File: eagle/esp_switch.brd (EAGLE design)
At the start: 100 x 80 mm, 20 parts, among them IC1 LT1117-3.3V

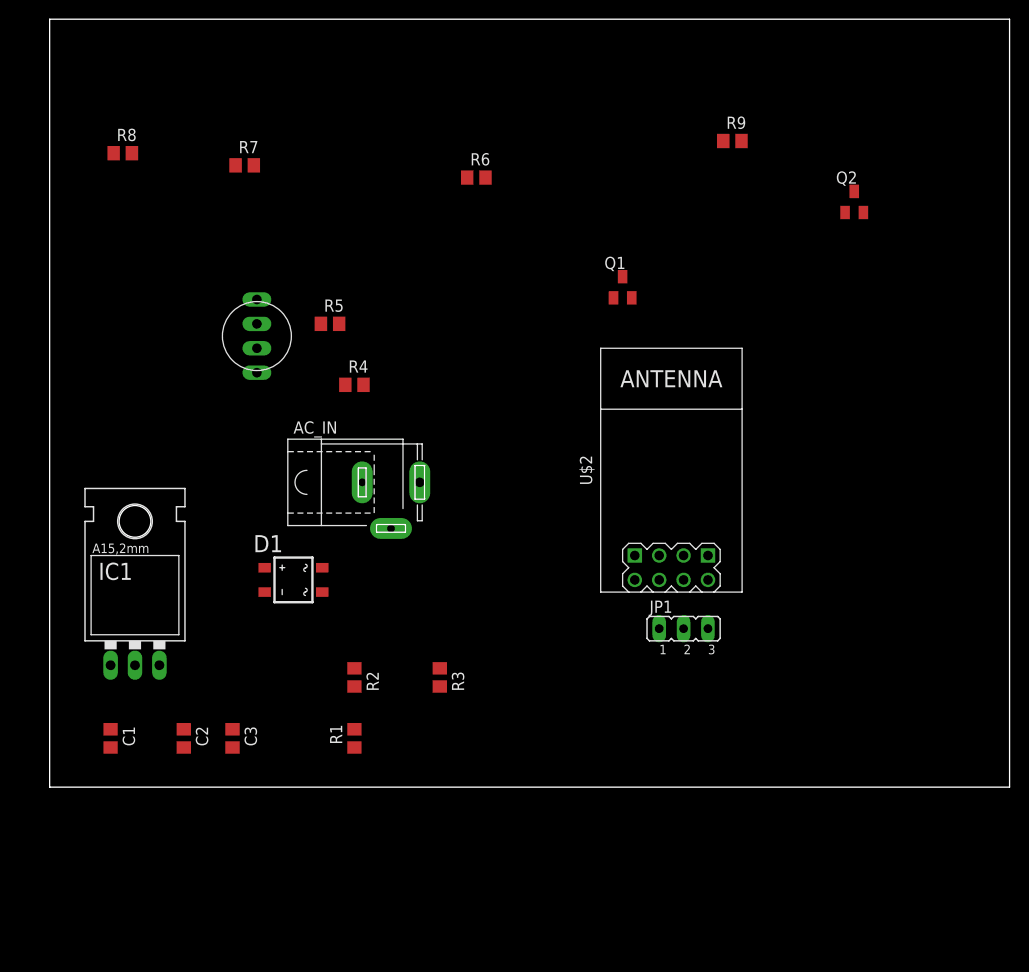
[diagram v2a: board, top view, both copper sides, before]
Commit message: modified brd size for case and add out port,SSR to sch, brd
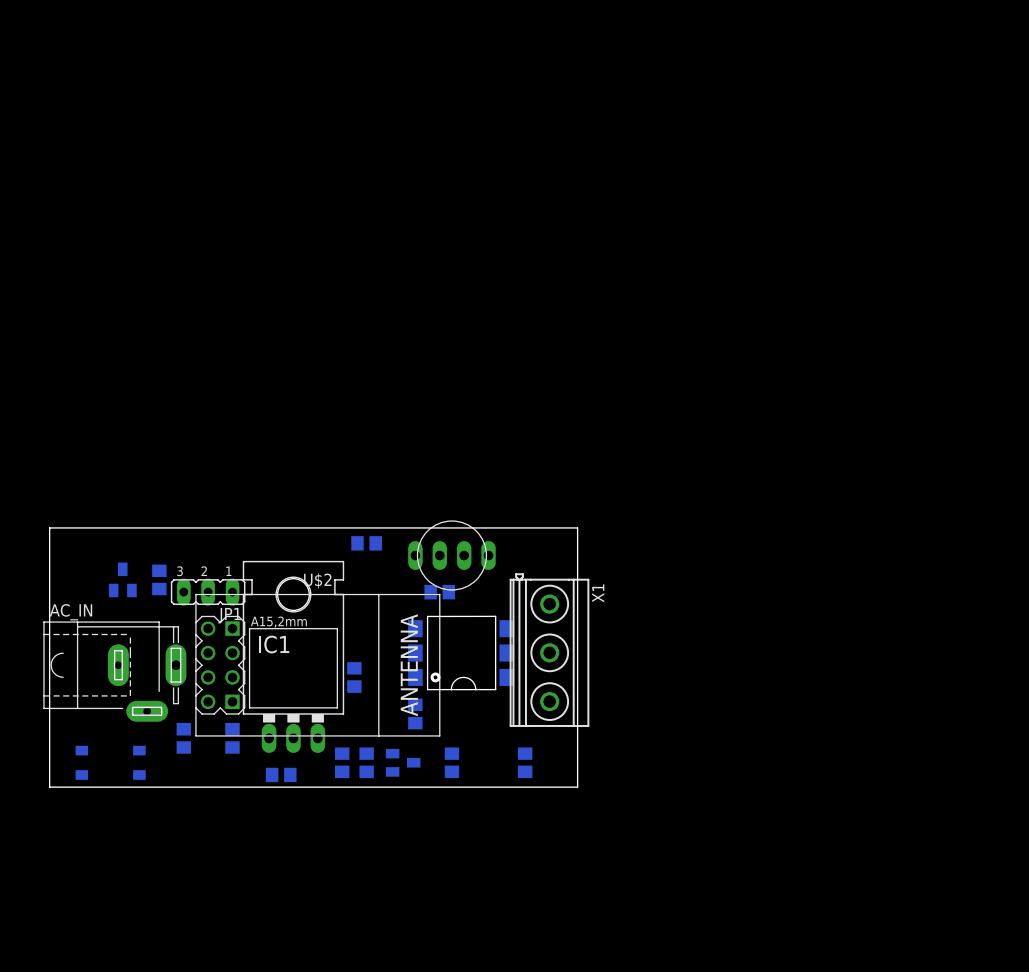
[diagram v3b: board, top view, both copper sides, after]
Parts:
- removed U$1: RGB_LEDA, covek:RGB_LED
- added LH1500: (no value), LH1500:LH1500
- added RGBLED5MM: RGB_LEDA, covek:RGB_LED
- added X1: MKDSN1,5/3-5,08, con-phoenix-508:MKDSN1,5/3-5,08
- AC_IN: value 6V AC -> 5V AC
- moved Q2 75.0 mm to (36.8, 2.54), flipped to the bottom, turned to 90 degrees
- moved R8 68.4 mm to (33.0, 2.54), flipped to the bottom, turned to 90 degrees
- moved R9 68.2 mm to (38.1, 7.62), flipped to the bottom, turned to 270 degrees
- moved R7 63.1 mm to (30.5, 2.54), flipped to the bottom, turned to 270 degrees
- moved Q1 60.3 mm to (7.62, 21.6), flipped to the bottom
- moved R6 53.4 mm to (11.4, 21.6), flipped to the bottom, turned to 90 degrees
- moved JP1 49.7 mm to (16.5, 20.3), turned to 180 degrees
- moved C1 43.3 mm to (49.5, 2.54), flipped to the bottom
- moved U$2 42.1 mm to (27.9, 12.7), turned to 0 degrees
- moved AC_IN 31.8 mm to (10.2, 12.7)
- moved D1 26.9 mm to (6.35, 2.54), flipped to the bottom
- moved R4 23.3 mm to (40.6, 20.3), flipped to the bottom
- moved R5 23.2 mm to (33.0, 25.4), flipped to the bottom
- moved IC1 18.2 mm to (25.4, 8.89)
- moved R3 8.98 mm to (41.9, 2.54), flipped to the bottom
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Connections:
- net N$7 renamed 3.3V
- new net 5V: AC_IN.3, D1.AC2
- new net N$18: LH1500.A, R9.1
- new net N$7: LH1500.DC, X1.2
- net N$1: now also D1.AC1; no longer D1.AC2
- net N$11: now also RGBLED5MM.P$2; no longer U$1.P$2
- net N$12: now also RGBLED5MM.P$4; no longer U$1.P$4
- net N$14: now also LH1500.S', X1.1; no longer Q2.2, R8.1
- net N$2: now also LH1500.S, X1.3; no longer AC_IN.3, D1.AC1
- net N$3: now also LH1500.C, RGBLED5MM.P$3
- net N$6: now also Q2.2, R8.1; no longer U$1.P$3
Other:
- board size 100 x 80 mm -> 55 x 27 mm

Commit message: brd modified2
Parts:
- moved X1 49.1 mm to (3.17, 15.9), turned to 90 degrees
- moved D1 38.9 mm to (45.1, 6.35), turned to 0 degrees
- moved AC_IN 34.9 mm to (45.1, 13.3), turned to 180 degrees
- moved R3 24.8 mm to (32.4, 25.4), turned to 180 degrees
- moved R7 24.3 mm to (22.2, 25.4), turned to 0 degrees
- moved JP1 24.1 mm to (36.2, 6.35), turned to 0 degrees
- moved LH1500 23.9 mm to (14.6, 15.9), turned to 0 degrees
- moved R8 23.6 mm to (27.3, 25.4), turned to 0 degrees
- moved C1 22.5 mm to (27.9, 8.89), turned to 90 degrees
- moved R9 21.3 mm to (18.4, 15.9), turned to 180 degrees
- moved Q2 18.9 mm to (23.5, 15.9), turned to 270 degrees
- moved R1 16.7 mm to (29.2, 17.1), turned to 0 degrees
- moved C2 9.67 mm to (22.9, 8.89), turned to 90 degrees
- moved R2 8.84 mm to (34.9, 19.7), turned to 180 degrees
- moved R5 8.54 mm to (39.4, 19.7)
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
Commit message: update sch and brd
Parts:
- removed IC1: LT1117-3.3V, v-reg:TO220L1
- added U$1: LD1117, LD1117:LD1117
- moved Q1 17.3 mm to (29.2, 22.2), turned to 270 degrees
- moved R6 17.2 mm to (33.7, 22.9)
- moved R1 11.8 mm to (38.7, 10.2), turned to 270 degrees
- moved R3 11.2 mm to (29.5, 14.6), turned to 0 degrees
- moved R8 9.71 mm to (25.4, 15.9), turned to 90 degrees
- moved R2 6.61 mm to (38.7, 14.3), turned to 90 degrees
- moved R7 5.46 mm to (25.4, 21.0), turned to 90 degrees
- moved C1 4.96 mm to (31.1, 5.08)
- moved R4 2.54 mm to (38.1, 22.9)
- moved R5 1.42 mm to (38.7, 18.4), turned to 270 degrees
- moved D1 1.27 mm to (45.1, 7.62)
- moved Q2 1.27 mm to (22.2, 15.9)
- moved R9 0.32 mm to (18.7, 15.9)
- turned RGBLED5MM to 180 degrees
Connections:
- net 5V renamed N$3
- removed net N$3 (its old number): C1.2, C2.2, C3.2, D1.-, IC1.1, JP1.1, LH1500.C, Q1.2, R1.1, RGBLED5MM.P$3, U$2.A1
- new net GND: C1.2, C2.2, C3.2, D1.-, JP1.1, LH1500.C, Q1.2, R1.1, RGBLED5MM.P$3, U$1.GND, U$2.A1
- net 3.3V: now also U$1.OUT; no longer IC1.2
- net N$6: now also U$1.IN; no longer IC1.3
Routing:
- net 3.3V: track 0.00 -> 52.2 mm, vias 0 -> 1
- net N$6: track 0.00 -> 39.4 mm
- net N$10: track 0.00 -> 18.6 mm, vias 0 -> 2
- net N$4: track 0.00 -> 18.0 mm
- net N$11: track 0.00 -> 11.8 mm
- net N$15: track 0.00 -> 5.25 mm
- net N$2: track 0.00 -> 4.47 mm
- net N$14: track 0.00 -> 4.47 mm
- net N$9: track 0.00 -> 3.81 mm
- net N$3: track 0.00 -> 3.54 mm
- net N$12: track 0.00 -> 3.50 mm
- net N$1: track 0.00 -> 3.35 mm
- net N$8: track 0.00 -> 3.18 mm
- net N$18: track 0.00 -> 3.18 mm
- net N$5: track 0.00 -> 3.18 mm
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- added copper zone on layer 16, net GND

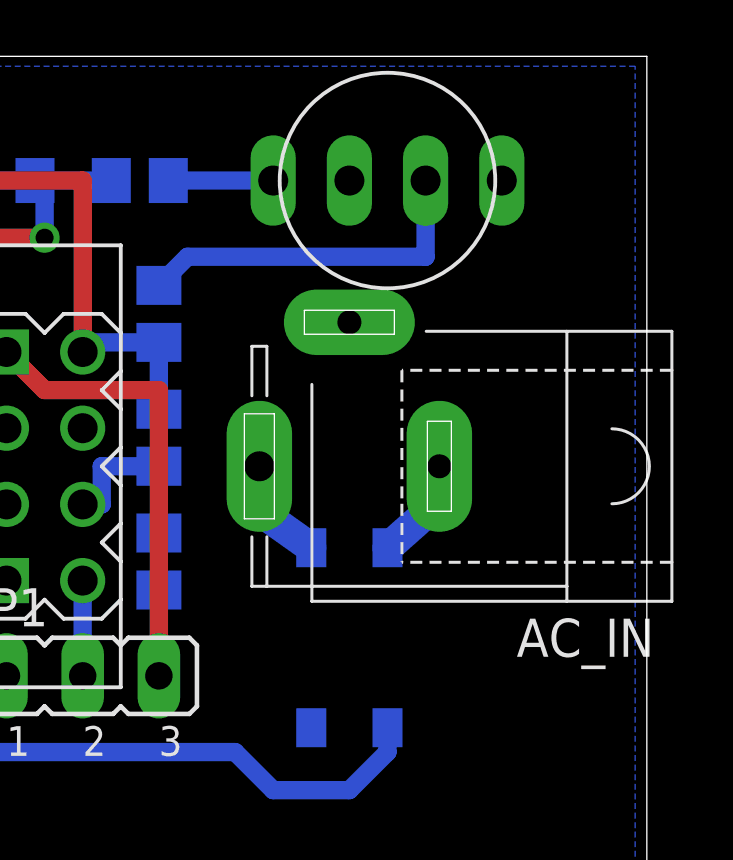
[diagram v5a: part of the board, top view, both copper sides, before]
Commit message: changed AC power connector, optimized milling
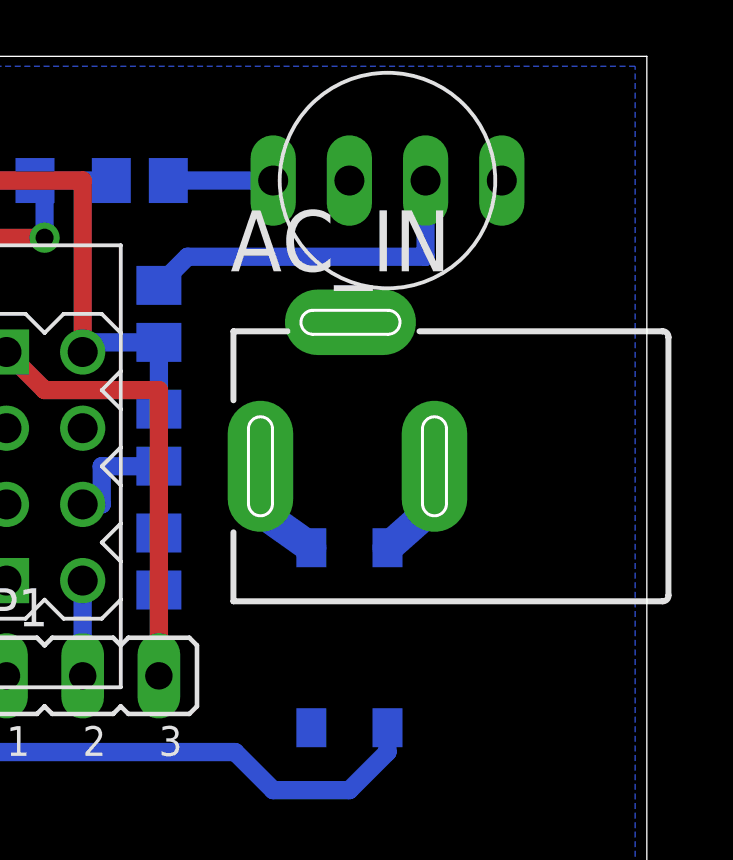
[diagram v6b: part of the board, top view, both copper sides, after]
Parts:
- AC_IN: value 5V AC -> (none); device con-jack:SPC4078 -> Wurth_Elektronik_Electromechanic_DC_Power_Jack_Connectors_rev16a_covek:694108301002
- moved AC_IN 10.6 mm to (55.7, 13.3), turned to 0 degrees
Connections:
- net N$1: now also AC_IN.2; no longer AC_IN.1
- net N$3: now also AC_IN.1; no longer AC_IN.3
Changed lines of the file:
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@@
 <?xml version="1.0" encoding="utf-8"?>
 <!DOCTYPE eagle SYSTEM "eagle.dtd">
-<eagle version="8.0.1">
+<eagle version="8.0.2">
 <drawing>
 <settings>
@@
 <layer number="44" name="Drills" color="7" fill="1" visible="no" active="yes"/>
 <layer number="45" name="Holes" color="7" fill="1" visible="no" active="yes"/>
-<layer number="46" name="Milling" color="3" fill="1" visible="no" active="yes"/>
+<layer number="46" name="Milling" color="3" fill="1" visible="yes" active="yes"/>
 <layer number="47" name="Measures" color="7" fill="1" visible="no" active="yes"/>
 <layer number="48" name="Document" color="7" fill="1" visible="yes" active="yes"/>
@@
 </autorouter>
 <elements>
-<element name="AC_IN" library="con-jack" package="SPC4078" value="5V AC" x="45.085" y="13.335" rot="R180">
-<attribute name="MF" value="" x="45.085" y="13.335" size="1.778" layer="27" rot="R180" display="off"/>
-<attribute name="MPN" value="" x="45.085" y="13.335" size="1.778" layer="27" rot="R180" display="off"/>
-<attribute name="OC_FARNELL" value="unknown" x="45.085" y="13.335" size="1.778" layer="27" rot="R180" display="off"/>
-<attribute name="OC_NEWARK" value="unknown" x="45.085" y="13.335" size="1.778" layer="27" rot="R180" display="off"/>
-</element>
 <element name="JP1" library="jumper" package="JP2" value="RS232_TTL" x="36.195" y="6.35"/>
 <element name="U$2" library="diy-modules" package="WIRELESS-WIFI-ESP-01" value="WIRELESS-WIFI-ESP-01" x="24.765" y="13.335" rot="R180"/>
@@
 <element name="X1" library="con-phoenix-508" package="MKDSN1,5/3-5,08" value="MKDSN1,5/3-5,08" x="3.175" y="15.875" rot="R90"/>
 <element name="U$1" library="LD1117" package="LD1117" value="LD1117" x="22.86" y="10.16"/>
+<element name="AC_IN" library="Wurth_Elektronik_Electromechanic_DC_Power_Jack_Connectors_rev16a_covek" package="694108301002" value="" x="55.72125" y="13.335"/>
 </elements>
 <signals>
@@
 <signal name="N$1">
 <contactref element="D1" pad="AC1"/>
+<wire x1="47.625" y1="11.7475" x2="46.355" y2="10.62" width="1.016" layer="16"/>
+<contactref element="AC_IN" pad="2"/>
+<wire x1="47.92125" y1="13.335" x2="47.625" y2="13.335" width="0.4064" layer="16"/>
+<wire x1="47.625" y1="13.335" x2="47.625" y2="11.7475" width="0.4064" layer="16"/>
+</signal>
+<signal name="N$3">
+<contactref element="D1" pad="AC2"/>
+<wire x1="42.2275" y1="11.7475" x2="43.815" y2="10.62" width="1.016" layer="16"/>
 <contactref element="AC_IN" pad="1"/>
-<wire x1="46.355" y1="10.62" x2="47.625" y2="11.7475" width="1.016" layer="16"/>
-<wire x1="47.625" y1="11.7475" x2="48.085" y2="13.335" width="1.016" layer="16"/>
-</signal>
-<signal name="N$3">
-<contactref element="AC_IN" pad="3"/>
-<contactref element="D1" pad="AC2"/>
-<wire x1="43.815" y1="10.62" x2="42.2275" y2="11.7475" width="1.016" layer="16"/>
-<wire x1="42.2275" y1="11.7475" x2="42.085" y2="13.335" width="1.016" layer="16"/>
+<wire x1="42.12125" y1="13.335" x2="42.2275" y2="13.335" width="0.4064" layer="16"/>
+<wire x1="42.2275" y1="13.335" x2="42.2275" y2="11.7475" width="0.4064" layer="16"/>
 </signal>
 </signals>
